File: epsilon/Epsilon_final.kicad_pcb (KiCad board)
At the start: 2 copper layers, 15 x 11 mm, 18 parts, among them J1 SGP+, J2 SGS+, J3 SGP-, J4 SGS-, J5 AudioJack4, U1 ADA4940-1ARZ-R7, U2 DS28E07P+T, U3 TCA9416DDFR

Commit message: Epsilon PCB Finished
Updated OZYS still WIP.
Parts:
- C4: moved to B.Cu
- moved U1 151.0 mm to (149.8, 86.8), turned to 180 degrees
- moved J5 139.1 mm to (144.1, 80.2)
- moved U2 138.9 mm to (142.0, 82.0)
- moved U3 138.3 mm to (137.0, 83.0), turned to 90 degrees
- moved C3 136.3 mm to (150.8, 83.4)
- moved R1 136.1 mm to (145.0, 87.0), turned to -90 degrees
- moved C2 136.1 mm to (150.5, 81.5)
- moved J1 135.3 mm to (143.5, 87.5)
- moved J2 135.3 mm to (141.0, 87.5)
- moved J3 135.3 mm to (138.5, 87.5)
- moved J4 135.3 mm to (136.0, 87.5)
- moved C1 133.9 mm to (150.5, 82.5), turned to 0 degrees
- moved R2 131.9 mm to (146.9, 84.5), turned to 180 degrees
- moved C4 131.8 mm to (136.0, 79.5), turned to 90 degrees
- moved D1 128.7 mm to (150.5, 79.0), turned to -90 degrees
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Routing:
- net GND: track 0.00 -> 40.9 mm, vias 0 -> 4
- net 3V3A_SW: track 0.00 -> 38.0 mm, vias 0 -> 3
- net Net-(D1-K): track 0.00 -> 24.6 mm, vias 0 -> 5
- net Net-(U1-–IN): track 0.00 -> 17.7 mm, vias 0 -> 3
- net Net-(U1-–OUT): track 0.00 -> 13.8 mm, vias 0 -> 1
- net Net-(U2-IO): track 0.00 -> 10.5 mm, vias 0 -> 2
- net Net-(U1-+IN): track 0.00 -> 8.23 mm, vias 0 -> 1
- net Net-(U1-+OUT): track 0.00 -> 4.14 mm, vias 0 -> 1
- net Net-(J4-Pin_1): track 0.00 -> 2.59 mm, vias 0 -> 1
- net Net-(J2-Pin_1): track 0.00 -> 2.17 mm, vias 0 -> 1
- net Net-(U1-VOCM): track 0.00 -> 2.08 mm, vias 0 -> 1
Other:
- board size 15 x 11 mm -> 17 x 12 mm

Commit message: add epsilon manufacturing files
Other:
- board text added: "Epsilon"
- board text added: "McMaster Rocketry"

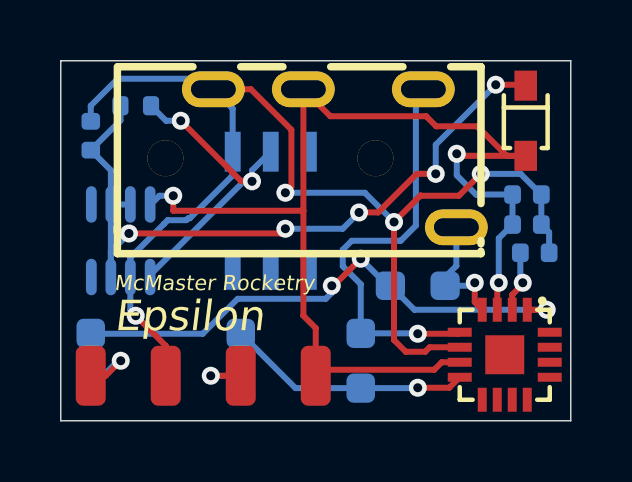
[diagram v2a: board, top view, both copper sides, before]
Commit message: Epsilon Symbol Fixed
Epsilon Symbol Fixed
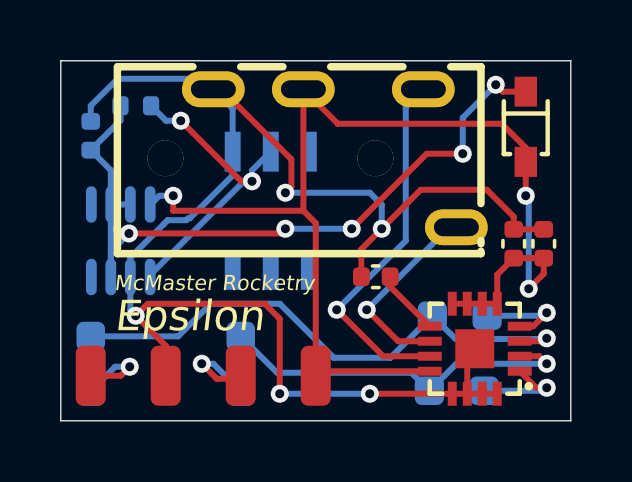
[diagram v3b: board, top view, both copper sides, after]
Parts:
- removed C1, C3: 100n, Capacitor_SMD:C_0402_1005Metric
- removed C2: 1000p, Capacitor_SMD:C_0402_1005Metric
- removed R1, R2: 330K, Resistor_SMD:R_0603_1608Metric_Pad0.98x0.95mm_HandSolder
- removed R3, R4: 6.8K, Resistor_SMD:R_0603_1608Metric_Pad0.98x0.95mm_HandSolder
- removed U1: ADA4940-1ARZ-R7, Rocketry_Easyeda:LFCSP-16_L3.0-W3.0-P0.50-BL-EP1.3
- added C5: 100n, Capacitor_SMD:C_0402_1005Metric, F.Cu at (150.1, 83.1)
- added C6: 1000p, Capacitor_SMD:C_0402_1005Metric, F.Cu at (151.1, 83.1)
- added C7: 100n, Capacitor_SMD:C_0402_1005Metric, F.Cu at (145.5, 84.2)
- added R5: 330K, Resistor_SMD:R_0603_1608Metric_Pad0.98x0.95mm_HandSolder, B.Cu at (148.2, 88.0)
- added R6: 330K, Resistor_SMD:R_0603_1608Metric_Pad0.98x0.95mm_HandSolder, B.Cu at (148.3, 85.5)
- added R8: 6.8K, Resistor_SMD:R_0603_1608Metric_Pad0.98x0.95mm_HandSolder, B.Cu at (141.0, 87.1)
- added R9: 6.8K, Resistor_SMD:R_0603_1608Metric_Pad0.98x0.95mm_HandSolder, B.Cu at (136.0, 87.1)
- added U4: ADA4940-1ACPZ-R7, Rocketry_Easyeda:LFCSP-16_L3.0-W3.0-P0.50-BL-EP1.3, F.Cu at (148.8, 86.6)
- moved D1 0.20 mm to (150.5, 79.2)
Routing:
- net Net-(U4--IN): track 0.00 -> 18.2 mm, vias 0 -> 1
- net Net-(U1-–IN): track 17.7 -> 0.00 mm, vias 3 -> 0
- net Net-(U4-+IN): track 0.00 -> 12.3 mm, vias 0 -> 1
- net GND: track 40.9 -> 51.3 mm, vias 4 -> 5
- net Net-(U1-+IN): track 8.23 -> 0.00 mm, vias 1 -> 0
- net Net-(U4-–FB): track 0.00 -> 3.26 mm, vias 0 -> 1
- net Net-(U4-+FB): track 0.00 -> 3.12 mm, vias 0 -> 1
- net Net-(U4-+OUT): track 4.14 -> 6.66 mm
- net Net-(U4-VOCM): track 0.00 -> 2.20 mm
- net Net-(U1-VOCM): track 2.08 -> 0.00 mm, vias 1 -> 0
- net Net-(U4--OUT): track 13.8 -> 12.3 mm
- net Net-(J2-Pin_1): track 2.17 -> 3.19 mm
